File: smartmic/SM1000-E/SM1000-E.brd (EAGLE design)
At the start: 65 x 100 mm, 200 parts, among them CN1 HDR100-3, CN10 ST-3509, CN11 HDR100-3, CN12 HRS-A3C-16DA, CN2 JS-MU3-002, CN3 DS-0518, CN4 RJ-45, CN5 ST-3509, CN6 ST-3509, CN7 ST-3509, CN8 ST-3509, CN9 ST-3509, J1 JMP-2PIN, J2 JMP-2PIN, J3 JMP-2PIN, J4 CONN-BOOM-XH-2A, P1 TPAD50, P10 TPAD50, P11 TPAD50, P12 TPAD50, P13 TPAD50, P14 TPAD50, P16 TPAD50, P18 TPAD50, P19 TPAD50, P2 TPAD50, P20 TPAD50, P3 TPAD50, P4 TPAD50, P5 TPAD50, P6 TPAD50, P7 TPAD50, P8 TPAD50, P9 TPAD50, SW1 SW-LC2259, SW2 TS-026, SW3 SW-LC2259EENP, SW4 TS-026, SW5 TS-02B, T1 SM-LP-5001, T2 SM-LP-5001, U1 STM32F405VGT6, U2 LD3985M33R, U3 STMPS2141, U4 EMIF02-USB03F2, U5 TPS54329E, U6 LMV341, U7 LMV341, U8 LM386M-1, U9 LMV341

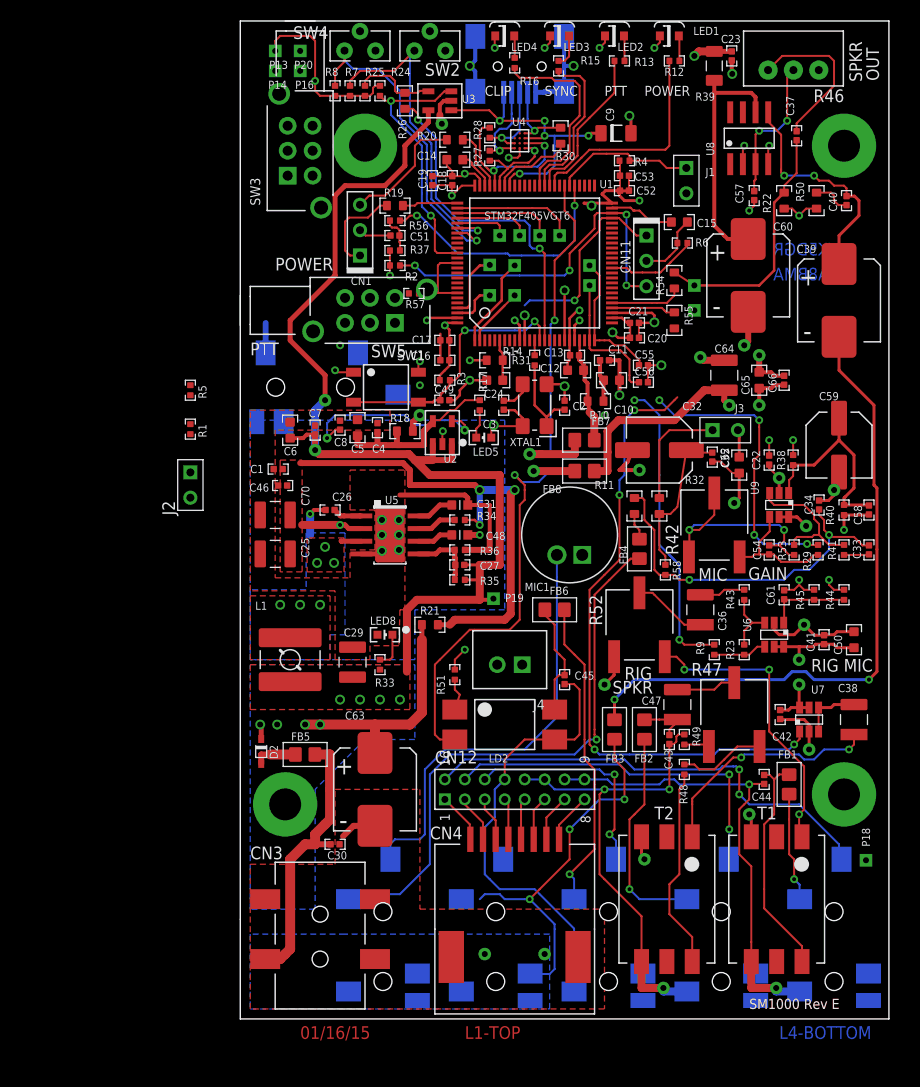
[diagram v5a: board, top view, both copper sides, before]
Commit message: 
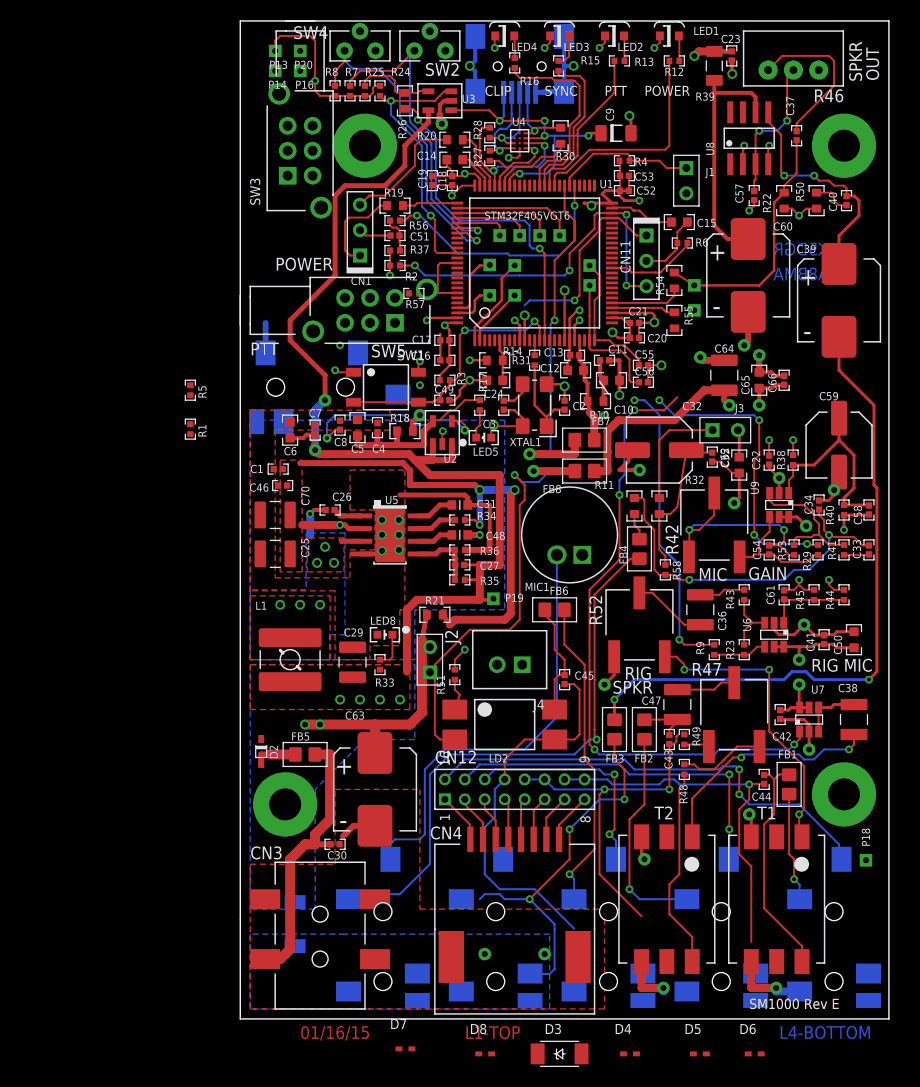
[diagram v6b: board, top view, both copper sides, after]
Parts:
- added D1: PTVS20VP1UP, _RoweTel:SOD128
- added D3: DNL, _RoweTel:SOD128
- added D4, D5, D6, D7, D8: DNL, _RoweTel:SOD523
- LED5: value (none) -> DNL
- moved J2 29.7 mm to (19.0, 36.0), turned to 180 degrees
- moved R21 1.12 mm to (19.5, 40.5)
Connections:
- removed net N$64: CN6.C, FB1.2
- new net N$84: CN6.C, D6.C, FB1.2
- net +VIN: now also SW3.3, SW3.6
- net APTT: now also D4.C
- net GND: now also D1.A, D3.A, D7.A, D8.A
- net N$15: now also D7.C
- net N$62: now also D3.C
- net N$70: now also D5.C
- net N$76: now also D8.C
- net N$77: now also D1.C
- net RF_MIC: now also D5.A
- net RF_PTT: now also D4.A
- net RF_SPKR: now also D6.A
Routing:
- net N$81: track 61.5 -> 0.00 mm, vias 2 -> 0
- net N$84: track 0.00 -> 11.0 mm, vias 0 -> 1
- net N$64: track 11.0 -> 0.00 mm, vias 1 -> 0
- net RF_MIC: track 48.4 -> 40.9 mm
- net RF_PTT: track 44.7 -> 38.3 mm
- net RF_SPKR: track 47.1 -> 45.2 mm
- net +VIN: track 159.1 -> 160.1 mm
